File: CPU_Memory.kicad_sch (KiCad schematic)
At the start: 1 part

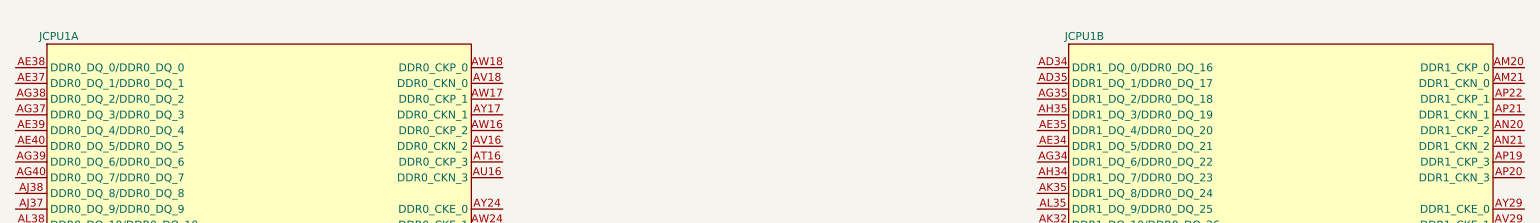
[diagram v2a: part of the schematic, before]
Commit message: Added first PCH symbol and footprint
THANKS @mothenjoyer69 so much for extracting and converting the PCH footprint from a laptop boardview ❤️
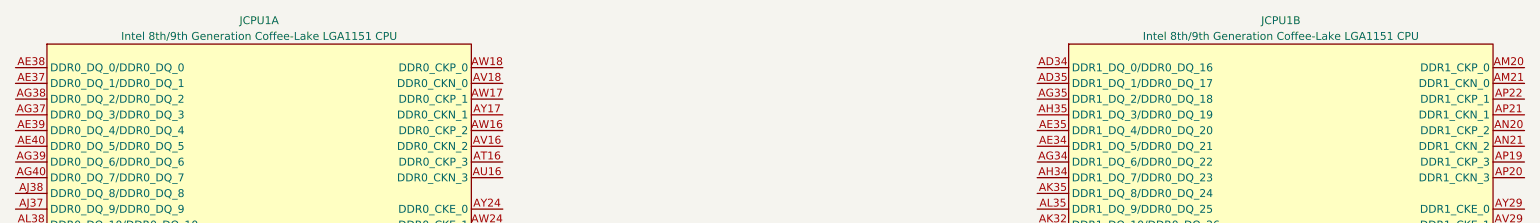
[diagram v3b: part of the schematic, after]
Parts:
- JCPU1: value ~ -> Intel 8th/9th Generation Coffee-Lake LGA1151 CPU

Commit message: Fixed some PCH pin names
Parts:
- added unit 2 of JCPU1

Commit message: Added sodimm memory slots and mostly hooked them up on the schematic
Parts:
- added JSODIMM1, JSODIMM2: DDR4-sodimm, A-my-stuff:DDR4-sodimm-std, symbol A-my-stuff:DDR4-sodimm
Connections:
- net DDR4_CH0_DQ1: now reaches JCPU1.AE37 (DDR0_DQ_1/DDR0_DQ_1)
- net DDR4_CH0_DQ1: now also JSODIMM1.7 (DQ1)
- net DDR4_CH0_DQ0: now reaches JCPU1.AE38 (DDR0_DQ_0/DDR0_DQ_0)
- net DDR4_CH0_DQ0: now also JSODIMM1.8 (DQ0)
- net DDR4_CH0_DQ4: now reaches JCPU1.AE39 (DDR0_DQ_4/DDR0_DQ_4)
- net DDR4_CH0_DQ4: now also JSODIMM1.4 (DQ4)
- net DDR4_CH0_DQ5: now reaches JCPU1.AE40 (DDR0_DQ_5/DDR0_DQ_5)
- net DDR4_CH0_DQ5: now also JSODIMM1.3 (DQ5)
- net DDR4_CH0_DQS0+: now reaches JCPU1.AF38 (DDR0_DQSP_0/DDR0_DQSP_0)
- net DDR4_CH0_DQS0+: now also JSODIMM1.13 (DQS0+)
- net DDR4_CH0_DQS0-: now reaches JCPU1.AF39 (DDR0_DQSN_0/DDR0_DQSN_0)
- net DDR4_CH0_DQS0-: now also JSODIMM1.11 (DQS0-)
- net DDR4_CH0_DQ3: now reaches JCPU1.AG37 (DDR0_DQ_3/DDR0_DQ_3)
- net DDR4_CH0_DQ3: now also JSODIMM1.21 (DQ3)
- net DDR4_CH0_DQ2: now reaches JCPU1.AG38 (DDR0_DQ_2/DDR0_DQ_2)
- net DDR4_CH0_DQ2: now also JSODIMM1.20 (DQ2)
- net DDR4_CH0_DQ6: now reaches JCPU1.AG39 (DDR0_DQ_6/DDR0_DQ_6)
- net DDR4_CH0_DQ6: now also JSODIMM1.16 (DQ6)
- net DDR4_CH0_DQ7: now reaches JCPU1.AG40 (DDR0_DQ_7/DDR0_DQ_7)
- net DDR4_CH0_DQ7: now also JSODIMM1.17 (DQ7)
- net DDR4_CH0_DQ57: now reaches JCPU1.AH1 (DDR0_DQ_57/DDR1_DQ_41)
- net DDR4_CH0_DQ57: now also JSODIMM1.236 (DQ57)
- net DDR4_CH0_DQ59: now reaches JCPU1.AH2 (DDR0_DQ_59/DDR1_DQ_43)
- net DDR4_CH0_DQ59: now also JSODIMM1.250 (DQ59)
- net DDR4_CH0_DQ62: now reaches JCPU1.AH3 (DDR0_DQ_62/DDR1_DQ_46)
- net DDR4_CH0_DQ62: now also JSODIMM1.245 (DQ62)
- net DDR4_CH0_DQ60: now reaches JCPU1.AH4 (DDR0_DQ_60/DDR1_DQ_44)
- net DDR4_CH0_DQ60: now also JSODIMM1.232 (DQ60)
- net DDR4_CH0_DQS7+: now reaches JCPU1.AJ2 (DDR0_DQSP_7/DDR1_DQSP_5)
- net DDR4_CH0_DQS7+: now also JSODIMM1.242 (DQS7+)
- net DDR4_CH0_DQS7-: now reaches JCPU1.AJ3 (DDR0_DQSN_7/DDR1_DQSN_5)
- net DDR4_CH0_DQS7-: now also JSODIMM1.240 (DQS7-)
- net DDR4_CH0_DQ9: now reaches JCPU1.AJ37 (DDR0_DQ_9/DDR0_DQ_9)
- net DDR4_CH0_DQ9: now also JSODIMM1.29 (DQ9)
- net DDR4_CH0_DQ8: now reaches JCPU1.AJ38 (DDR0_DQ_8/DDR0_DQ_8)
- net DDR4_CH0_DQ8: now also JSODIMM1.28 (DQ8)
- net DDR4_CH0_DQ13: now reaches JCPU1.AJ39 (DDR0_DQ_13/DDR0_DQ_13)
- net DDR4_CH0_DQ13: now also JSODIMM1.25 (DQ13)
- net DDR4_CH0_DQ12: now reaches JCPU1.AJ40 (DDR0_DQ_12/DDR0_DQ_12)
- net DDR4_CH0_DQ12: now also JSODIMM1.24 (DQ12)
- net DDR4_CH0_DQ63: now reaches JCPU1.AK1 (DDR0_DQ_63/DDR1_DQ_47)
- net DDR4_CH0_DQ63: now also JSODIMM1.246 (DQ63)
- net DDR4_CH0_DQ61: now reaches JCPU1.AK2 (DDR0_DQ_61/DDR1_DQ_45)
- net DDR4_CH0_DQ61: now also JSODIMM1.233 (DQ61)
- net DDR4_CH0_DQ56: now reaches JCPU1.AK3 (DDR0_DQ_56/DDR1_DQ_40)
- net DDR4_CH0_DQ56: now also JSODIMM1.237 (DQ56)
- net DDR4_CH0_DQS1+: now reaches JCPU1.AK38 (DDR0_DQSP_1/DDR0_DQSP_1)
- net DDR4_CH0_DQS1+: now also JSODIMM1.34 (DQS1+)
- net DDR4_CH0_DQS1-: now reaches JCPU1.AK39 (DDR0_DQSN_1/DDR0_DQSN_1)
- net DDR4_CH0_DQS1-: now also JSODIMM1.32 (DQS1-)
- net DDR4_CH0_DQ58: now reaches JCPU1.AK4 (DDR0_DQ_58/DDR1_DQ_42)
- net DDR4_CH0_DQ58: now also JSODIMM1.249 (DQ58)
- net DDR4_CH0_DQ11: now reaches JCPU1.AL37 (DDR0_DQ_11/DDR0_DQ_11)
- net DDR4_CH0_DQ11: now also JSODIMM1.42 (DQ11)
- net DDR4_CH0_DQ10: now reaches JCPU1.AL38 (DDR0_DQ_10/DDR0_DQ_10)
- net DDR4_CH0_DQ10: now also JSODIMM1.41 (DQ10)
- net DDR4_CH0_DQ14: now reaches JCPU1.AL39 (DDR0_DQ_14/DDR0_DQ_14)
- net DDR4_CH0_DQ14: now also JSODIMM1.38 (DQ14)
- net DDR4_CH0_DQ15: now reaches JCPU1.AL40 (DDR0_DQ_15/DDR0_DQ_15)
- net DDR4_CH0_DQ15: now also JSODIMM1.37 (DQ15)
- net DDR4_CH0_DQ55: now reaches JCPU1.AM1 (DDR0_DQ_55/DDR1_DQ_39)
- net DDR4_CH0_DQ55: now also JSODIMM1.225 (DQ55)
- net DDR4_CH0_DQ53: now reaches JCPU1.AM2 (DDR0_DQ_53/DDR1_DQ_37)
- net DDR4_CH0_DQ53: now also JSODIMM1.212 (DQ53)
- net DDR4_CH0_DQ51: now reaches JCPU1.AM3 (DDR0_DQ_51/DDR1_DQ_35)
- net DDR4_CH0_DQ51: now also JSODIMM1.229 (DQ51)
- net DDR4_CH0_DQ49: now reaches JCPU1.AM4 (DDR0_DQ_49/DDR1_DQ_33)
- net DDR4_CH0_DQ49: now also JSODIMM1.215 (DQ49)
- net DDR4_CH0_DQS6+: now reaches JCPU1.AN2 (DDR0_DQSP_6/DDR1_DQSP_4)
- net DDR4_CH0_DQS6+: now also JSODIMM1.221 (DQS6+)
- net DDR4_CH0_DQS6-: now reaches JCPU1.AN3 (DDR0_DQSN_6/DDR1_DQSN_4)
- net DDR4_CH0_DQS6-: now also JSODIMM1.219 (DQS6-)
- net DDR4_CH0_DQ21: now reaches JCPU1.AN37 (DDR0_DQ_21/DDR0_DQ_37)
- net DDR4_CH0_DQ21: now also JSODIMM1.45 (DQ21)
- net DDR4_CH0_DQ16: now reaches JCPU1.AN38 (DDR0_DQ_16/DDR0_DQ_32)
- net DDR4_CH0_DQ16: now also JSODIMM1.50 (DQ16)
- net DDR4_CH0_DQ20: now reaches JCPU1.AN39 (DDR0_DQ_20/DDR0_DQ_36)
- net DDR4_CH0_DQ20: now also JSODIMM1.46 (DQ20)
- net DDR4_CH0_DQ17: now reaches JCPU1.AN40 (DDR0_DQ_17/DDR0_DQ_33)
- net DDR4_CH0_DQ17: now also JSODIMM1.49 (DQ17)
- net DDR4_CH0_DQ54: now reaches JCPU1.AP1 (DDR0_DQ_54/DDR1_DQ_38)
- net DDR4_CH0_DQ54: now also JSODIMM1.224 (DQ54)
- net DDR4_CH0_DQ48: now reaches JCPU1.AP2 (DDR0_DQ_48/DDR1_DQ_32)
- net DDR4_CH0_DQ48: now also JSODIMM1.216 (DQ48)
- net DDR4_CH0_DQ50: now reaches JCPU1.AP3 (DDR0_DQ_50/DDR1_DQ_34)
- net DDR4_CH0_DQ50: now also JSODIMM1.228 (DQ50)
- net DDR4_CH0_DQS2+: now reaches JCPU1.AP38 (DDR0_DQSP_2/DDR0_DQSP_4)
- net DDR4_CH0_DQS2+: now also JSODIMM1.55 (DQS2+)
- net DDR4_CH0_DQS2-: now reaches JCPU1.AP39 (DDR0_DQSN_2/DDR0_DQSN_4)
- net DDR4_CH0_DQS2-: now also JSODIMM1.53 (DQS2-)
- net DDR4_CH0_DQ52: now reaches JCPU1.AP4 (DDR0_DQ_52/DDR1_DQ_36)
- net DDR4_CH0_DQ52: now also JSODIMM1.211 (DQ52)
- net DDR4_CH0_DQ19: now reaches JCPU1.AR37 (DDR0_DQ_19/DDR0_DQ_35)
- net DDR4_CH0_DQ19: now also JSODIMM1.63 (DQ19)
- net DDR4_CH0_DQ18: now reaches JCPU1.AR38 (DDR0_DQ_18/DDR0_DQ_34)
- net DDR4_CH0_DQ18: now also JSODIMM1.62 (DQ18)
- net DDR4_CH0_DQ22: now reaches JCPU1.AR39 (DDR0_DQ_22/DDR0_DQ_38)
- net DDR4_CH0_DQ22: now also JSODIMM1.58 (DQ22)
- net DDR4_CH0_DQ23: now reaches JCPU1.AR40 (DDR0_DQ_23/DDR0_DQ_39)
- net DDR4_CH0_DQ23: now also JSODIMM1.59 (DQ23)
- net DDR4_CH0_DQ42: now reaches JCPU1.AT1 (DDR0_DQ_42/DDR1_DQ_10)
- net DDR4_CH0_DQ42: now also JSODIMM1.207 (DQ42)
- net DDR4_CH0_A4: now reaches JCPU1.AT19 (DDR0_MA_4)
- net DDR4_CH0_A4: now also JSODIMM1.128 (A4)
- net DDR4_CH0_DQ43: now reaches JCPU1.AT2 (DDR0_DQ_43/DDR1_DQ_11)
- net DDR4_CH0_DQ43: now also JSODIMM1.208 (DQ43)
- net DDR4_CH0_A8: now reaches JCPU1.AT20 (DDR0_MA_8)
- net DDR4_CH0_A8: now also JSODIMM1.125 (A8)
- net DDR4_CH0_A9: now reaches JCPU1.AT22 (DDR0_MA_9)
- net DDR4_CH0_A9: now also JSODIMM1.121 (A9)
- net DDR4_CH0_Alert#: now reaches JCPU1.AT23 (DDR0_ALERT#)
- net DDR4_CH0_Alert#: now also JSODIMM1.116 (ALERT#)
- net DDR4_CH0_DQ47: now reaches JCPU1.AT3 (DDR0_DQ_47/DDR1_DQ_15)
- net DDR4_CH0_DQ47: now also JSODIMM1.204 (DQ47)
- net DDR4_CH0_ECC1: now reaches JCPU1.AT33 (DDR0_ECC_1)
- net DDR4_CH0_ECC1: now also JSODIMM1.91 (CB1)
- net DDR4_CH0_DQ30: now reaches JCPU1.AT35 (DDR0_DQ_30/DDR0_DQ_46)
- net DDR4_CH0_DQ30: now also JSODIMM1.79 (DQ30)
- net DDR4_CH0_DQ46: now reaches JCPU1.AT4 (DDR0_DQ_46/DDR1_DQ_14)
- net DDR4_CH0_DQ46: now also JSODIMM1.203 (DQ46)
- net DDR4_CH0_CS1#: now reaches JCPU1.AU11 (DDR0_CS#_1)
- net DDR4_CH0_CS1#: now also JSODIMM1.157 (CS1#)
- net DDR4_CH0_ODT1: now reaches JCPU1.AU14 (DDR0_ODT_1)
- net DDR4_CH0_ODT1: now also JSODIMM1.161 (ODT1)
- net DDR4_CH0_A2: now reaches JCPU1.AU17 (DDR0_MA_2)
- net DDR4_CH0_A2: now also JSODIMM1.132 (A2)
- net DDR4_CH0_A1: now reaches JCPU1.AU18 (DDR0_MA_1)
- net DDR4_CH0_A1: now also JSODIMM1.133 (A1)
- net DDR4_CH0_DQS5+: now reaches JCPU1.AU2 (DDR0_DQSP_5/DDR1_DQSP_1)
- net DDR4_CH0_DQS5+: now also JSODIMM1.200 (DQS5+)
- net DDR4_CH0_A5: now reaches JCPU1.AU20 (DDR0_MA_5)
- net DDR4_CH0_A5: now also JSODIMM1.126 (A5)
- net DDR4_CH0_A7: now reaches JCPU1.AU21 (DDR0_MA_7)
- net DDR4_CH0_A7: now also JSODIMM1.122 (A7)
- net DDR4_CH0_A11: now reaches JCPU1.AU22 (DDR0_MA_11)
- net DDR4_CH0_A11: now also JSODIMM1.120 (A11)
- net DDR4_CH0_ACT#: now reaches JCPU1.AU24 (DDR0_ACT#)
- net DDR4_CH0_ACT#: now also JSODIMM1.114 (ACT#)
- net DDR4_CH0_DQS5-: now reaches JCPU1.AU3 (DDR0_DQSN_5/DDR1_DQSN_1)
- net DDR4_CH0_DQS5-: now also JSODIMM1.198 (DQS5-)
- net DDR4_CH0_ECC4: now reaches JCPU1.AU31 (DDR0_ECC_4)
- net DDR4_CH0_ECC4: now also JSODIMM1.88 (CB4)
- net DDR4_CH0_DQS8-: now reaches JCPU1.AU32 (DDR0_DQSN_8/DDR0_DQSN_8)
- net DDR4_CH0_DQS8-: now also JSODIMM1.95 (DQS8-)
- net DDR4_CH0_ECC0: now reaches JCPU1.AU33 (DDR0_ECC_0)
- net DDR4_CH0_ECC0: now also JSODIMM1.92 (CB0)
- net DDR4_CH0_DQ31: now reaches JCPU1.AU35 (DDR0_DQ_31/DDR0_DQ_47)
- net DDR4_CH0_DQ31: now also JSODIMM1.80 (DQ31)
- net DDR4_CH0_DQS3-: now reaches JCPU1.AU36 (DDR0_DQSN_3/DDR0_DQSN_5)
- net DDR4_CH0_DQS3-: now also JSODIMM1.74 (DQS3-)
- net DDR4_CH0_DQ28: now reaches JCPU1.AU37 (DDR0_DQ_28/DDR0_DQ_44)
- net DDR4_CH0_DQ28: now also JSODIMM1.66 (DQ28)
- net DDR4_CH0_DQ25: now reaches JCPU1.AU38 (DDR0_DQ_25/DDR0_DQ_41)
- net DDR4_CH0_DQ25: now also JSODIMM1.71 (DQ25)
- net DDR4_CH0_DQ35: now reaches JCPU1.AU6 (DDR0_DQ_35/DDR1_DQ_3)
- net DDR4_CH0_DQ35: now also JSODIMM1.186 (DQ35)
- net DDR4_CH0_DQ36: now reaches JCPU1.AU8 (DDR0_DQ_36/DDR1_DQ_4)
- net DDR4_CH0_DQ36: now also JSODIMM1.170 (DQ36)
- net DDR4_CH0_A13: now reaches JCPU1.AV12 (DDR0_MA_13)
- net DDR4_CH0_A13: now also JSODIMM1.158 (A13)
- net DDR4_CH0_A14_WE#: now reaches JCPU1.AV14 (DDR0_MA_14)
- net DDR4_CH0_A14_WE#: now also JSODIMM1.151 (A14/WE#)
- net DDR4_CH0_BA1: now reaches JCPU1.AV15 (DDR0_BA_1)
- net DDR4_CH0_BA1: now also JSODIMM1.145 (BA1)
- net DDR4_CH0_CLK0-: now reaches JCPU1.AV18 (DDR0_CKN_0)
- net DDR4_CH0_CLK0-: now also JSODIMM1.139 (CK0-)
- net DDR4_CH0_A3: now reaches JCPU1.AV19 (DDR0_MA_3)
- net DDR4_CH0_A3: now also JSODIMM1.131 (A3)
- net DDR4_CH0_A6: now reaches JCPU1.AV20 (DDR0_MA_6)
- net DDR4_CH0_A6: now also JSODIMM1.127 (A6)
- net DDR4_CH0_A12: now reaches JCPU1.AV22 (DDR0_MA_12)
- net DDR4_CH0_A12: now also JSODIMM1.119 (A12/BC#)
- net DDR4_CH0_BG1: now reaches JCPU1.AV23 (DDR0_BG_1)
- net DDR4_CH0_BG1: now also JSODIMM1.113 (BG1)
- net DDR4_CH0_DQ44: now reaches JCPU1.AV3 (DDR0_DQ_44/DDR1_DQ_12)
- net DDR4_CH0_DQ44: now also JSODIMM1.191 (DQ44)
- net DDR4_CH0_ECC3: now reaches JCPU1.AV31 (DDR0_ECC_3)
- net DDR4_CH0_ECC3: now also JSODIMM1.105 (CB3)
- net DDR4_CH0_DQS8+: now reaches JCPU1.AV32 (DDR0_DQSP_8/DDR0_DQSP_8)
- net DDR4_CH0_DQS8+: now also JSODIMM1.97 (DQS8+)
- net DDR4_CH0_ECC5: now reaches JCPU1.AV33 (DDR0_ECC_5)
- net DDR4_CH0_ECC5: now also JSODIMM1.87 (CB5)
- net DDR4_CH0_DQ26: now reaches JCPU1.AV35 (DDR0_DQ_26/DDR0_DQ_42)
- net DDR4_CH0_DQ26: now also JSODIMM1.83 (DQ26)
- net DDR4_CH0_DQS3+: now reaches JCPU1.AV36 (DDR0_DQSP_3/DDR0_DQSP_5)
- net DDR4_CH0_DQS3+: now also JSODIMM1.76 (DQS3+)
- net DDR4_CH0_DQ29: now reaches JCPU1.AV37 (DDR0_DQ_29/DDR0_DQ_45)
- net DDR4_CH0_DQ29: now also JSODIMM1.67 (DQ29)
- net DDR4_CH0_DQ41: now reaches JCPU1.AV4 (DDR0_DQ_41/DDR1_DQ_9)
- net DDR4_CH0_DQ41: now also JSODIMM1.194 (DQ41)
- net DDR4_CH0_DQ34: now reaches JCPU1.AV6 (DDR0_DQ_34/DDR1_DQ_2)
- net DDR4_CH0_DQ34: now also JSODIMM1.187 (DQ34)
- net DDR4_CH0_DQS4+: now reaches JCPU1.AV7 (DDR0_DQSP_4/DDR1_DQSP_0)
- net DDR4_CH0_DQS4+: now also JSODIMM1.179 (DQS4+)
- net DDR4_CH0_DQ37: now reaches JCPU1.AV8 (DDR0_DQ_37/DDR1_DQ_5)
- net DDR4_CH0_DQ37: now also JSODIMM1.169 (DQ37)
- net DDR4_CH0_ODT0: now reaches JCPU1.AW11 (DDR0_ODT_0)
- net DDR4_CH0_ODT0: now also JSODIMM1.155 (ODT0)
- net DDR4_CH0_CS0#: now reaches JCPU1.AW12 (DDR0_CS#_0)
- net DDR4_CH0_CS0#: now also JSODIMM1.149 (CS0#)
- net DDR4_CH0_A16_RAS#: now reaches JCPU1.AW13 (DDR0_MA_16)
- net DDR4_CH0_A16_RAS#: now also JSODIMM1.152 (A16/RAS#)
- net DDR4_CH0_A0: now reaches JCPU1.AW15 (DDR0_MA_0)
- net DDR4_CH0_A0: now also JSODIMM1.144 (A0)
- net DDR4_CH0_CLK1+: now reaches JCPU1.AW17 (DDR0_CKP_1)
- net DDR4_CH0_CLK1+: now also JSODIMM1.138 (CK1+)
- net DDR4_CH0_CLK0+: now reaches JCPU1.AW18 (DDR0_CKP_0)
- net DDR4_CH0_CLK0+: now also JSODIMM1.137 (CK0+)
- net DDR4_CH0_BG0: now reaches JCPU1.AW23 (DDR0_BG_0)
- net DDR4_CH0_BG0: now also JSODIMM1.115 (BG0)
- net DDR4_CH0_CKE1: now reaches JCPU1.AW24 (DDR0_CKE_1)
- net DDR4_CH0_CKE1: now also JSODIMM1.110 (CKE1)
- net DDR4_CH0_ECC6: now reaches JCPU1.AW31 (DDR0_ECC_6)
- net DDR4_CH0_ECC6: now also JSODIMM1.100 (CB6)
- net DDR4_CH0_ECC2: now reaches JCPU1.AW33 (DDR0_ECC_2)
- net DDR4_CH0_ECC2: now also JSODIMM1.101 (CB2)
- net DDR4_CH0_DQ27: now reaches JCPU1.AW35 (DDR0_DQ_27/DDR0_DQ_43)
- net DDR4_CH0_DQ27: now also JSODIMM1.84 (DQ27)
- net DDR4_CH0_DQ24: now reaches JCPU1.AW37 (DDR0_DQ_24/DDR0_DQ_40)
- net DDR4_CH0_DQ24: now also JSODIMM1.70 (DQ24)
- net DDR4_CH0_DQ45: now reaches JCPU1.AW4 (DDR0_DQ_45/DDR1_DQ_13)
- net DDR4_CH0_DQ45: now also JSODIMM1.190 (DQ45)
- net DDR4_CH0_DQ38: now reaches JCPU1.AW6 (DDR0_DQ_38/DDR1_DQ_6)
- net DDR4_CH0_DQ38: now also JSODIMM1.183 (DQ38)
- net DDR4_CH0_DQS4-: now reaches JCPU1.AW7 (DDR0_DQSN_4/DDR1_DQSN_0)
- net DDR4_CH0_DQS4-: now also JSODIMM1.177 (DQS4-)
- net DDR4_CH0_DQ33: now reaches JCPU1.AW8 (DDR0_DQ_33/DDR1_DQ_1)
- net DDR4_CH0_DQ33: now also JSODIMM1.173 (DQ33)
- net DDR4_CH0_A15_CAS#: now reaches JCPU1.AY11 (DDR0_MA_15)
- net DDR4_CH0_A15_CAS#: now also JSODIMM1.156 (A15/CAS#)
- net DDR4_CH0_BA0: now reaches JCPU1.AY13 (DDR0_BA_0)
- net DDR4_CH0_BA0: now also JSODIMM1.150 (BA0)
- net DDR4_CH0_A10: now reaches JCPU1.AY14 (DDR0_MA_10)
- net DDR4_CH0_A10: now also JSODIMM1.146 (A10/AP)
- net DDR4_CH0_Parity: now reaches JCPU1.AY15 (DDR0_PAR)
- net DDR4_CH0_Parity: now also JSODIMM1.143 (PARITY)
- net DDR4_CH0_CLK1-: now reaches JCPU1.AY17 (DDR0_CKN_1)
- net DDR4_CH0_CLK1-: now also JSODIMM1.140 (CK1-)
- net DDR4_CH0_CKE0: now reaches JCPU1.AY24 (DDR0_CKE_0)
- net DDR4_CH0_CKE0: now also JSODIMM1.109 (CKE0)
- net DDR4_CH0_ECC7: now reaches JCPU1.AY31 (DDR0_ECC_7)
- net DDR4_CH0_ECC7: now also JSODIMM1.104 (CB7)
- net DDR4_CH0_DQ40: now reaches JCPU1.AY4 (DDR0_DQ_40/DDR1_DQ_8)
- net DDR4_CH0_DQ40: now also JSODIMM1.195 (DQ40)
- net DDR4_CH0_DQ39: now reaches JCPU1.AY6 (DDR0_DQ_39/DDR1_DQ_7)
- net DDR4_CH0_DQ39: now also JSODIMM1.182 (DQ39)
- net DDR4_CH0_DQ32: now reaches JCPU1.AY8 (DDR0_DQ_32/DDR1_DQ_0)
- net DDR4_CH0_DQ32: now also JSODIMM1.174 (DQ32)
- net DDR4_CH1_DQ0: now reaches JCPU1.AD34 (DDR1_DQ_0/DDR0_DQ_16)
- net DDR4_CH1_DQ0: now also JSODIMM2.8 (DQ0)
- net DDR4_CH1_DQ1: now reaches JCPU1.AD35 (DDR1_DQ_1/DDR0_DQ_17)
- net DDR4_CH1_DQ1: now also JSODIMM2.7 (DQ1)
- net DDR4_CH1_DQ5: now reaches JCPU1.AE34 (DDR1_DQ_5/DDR0_DQ_21)
- net DDR4_CH1_DQ5: now also JSODIMM2.3 (DQ5)
- net DDR4_CH1_DQ4: now reaches JCPU1.AE35 (DDR1_DQ_4/DDR0_DQ_20)
- net DDR4_CH1_DQ4: now also JSODIMM2.4 (DQ4)
- net DDR4_CH1_DQ58: now reaches JCPU1.AE6 (DDR1_DQ_58/DDR1_DQ_58)
- net DDR4_CH1_DQ58: now also JSODIMM2.249 (DQ58)
- net DDR4_CH1_DQ62: now reaches JCPU1.AE7 (DDR1_DQ_62/DDR1_DQ_62)
- net DDR4_CH1_DQ62: now also JSODIMM2.245 (DQ62)
- net DDR4_CH1_DQS0-: now reaches JCPU1.AF34 (DDR1_DQSN_0/DDR0_DQSN_2)
- net DDR4_CH1_DQS0-: now also JSODIMM2.11 (DQS0-)
- net DDR4_CH1_DQS0+: now reaches JCPU1.AF35 (DDR1_DQSP_0/DDR0_DQSP_2)
- net DDR4_CH1_DQS0+: now also JSODIMM2.13 (DQS0+)
- net DDR4_CH1_DQ63: now reaches JCPU1.AF6 (DDR1_DQ_63/DDR1_DQ_63)
- net DDR4_CH1_DQ63: now also JSODIMM2.246 (DQ63)
- net DDR4_CH1_DQ59: now reaches JCPU1.AF7 (DDR1_DQ_59/DDR1_DQ_59)
- net DDR4_CH1_DQ59: now also JSODIMM2.250 (DQ59)
- net DDR4_CH1_DQ6: now reaches JCPU1.AG34 (DDR1_DQ_6/DDR0_DQ_22)
- net DDR4_CH1_DQ6: now also JSODIMM2.16 (DQ6)
- net DDR4_CH1_DQ2: now reaches JCPU1.AG35 (DDR1_DQ_2/DDR0_DQ_18)
- net DDR4_CH1_DQ2: now also JSODIMM2.20 (DQ2)
- net DDR4_CH1_DQS7-: now reaches JCPU1.AG6 (DDR1_DQSN_7/DDR1_DQSN_7)
- net DDR4_CH1_DQS7-: now also JSODIMM2.240 (DQS7-)
- net DDR4_CH1_DQS7+: now reaches JCPU1.AG7 (DDR1_DQSP_7/DDR1_DQSP_7)
- net DDR4_CH1_DQS7+: now also JSODIMM2.242 (DQS7+)
- net DDR4_CH1_DQ7: now reaches JCPU1.AH34 (DDR1_DQ_7/DDR0_DQ_23)
- net DDR4_CH1_DQ7: now also JSODIMM2.17 (DQ7)
- net DDR4_CH1_DQ3: now reaches JCPU1.AH35 (DDR1_DQ_3/DDR0_DQ_19)
- net DDR4_CH1_DQ3: now also JSODIMM2.21 (DQ3)
- net DDR4_CH1_DQ61: now reaches JCPU1.AH6 (DDR1_DQ_61/DDR1_DQ_61)
- net DDR4_CH1_DQ61: now also JSODIMM2.233 (DQ61)
- net DDR4_CH1_DQ60: now reaches JCPU1.AH7 (DDR1_DQ_60/DDR1_DQ_60)
- net DDR4_CH1_DQ60: now also JSODIMM2.232 (DQ60)
- net DDR4_CH1_DQ56: now reaches JCPU1.AJ6 (DDR1_DQ_56/DDR1_DQ_56)
- net DDR4_CH1_DQ56: now also JSODIMM2.237 (DQ56)
- net DDR4_CH1_DQ57: now reaches JCPU1.AJ7 (DDR1_DQ_57/DDR1_DQ_57)
- net DDR4_CH1_DQ57: now also JSODIMM2.236 (DQ57)
- net DDR4_CH1_DQ14: now reaches JCPU1.AK31 (DDR1_DQ_14/DDR0_DQ_30)
- net DDR4_CH1_DQ14: now also JSODIMM2.38 (DQ14)
- net DDR4_CH1_DQ10: now reaches JCPU1.AK32 (DDR1_DQ_10/DDR0_DQ_26)
- net DDR4_CH1_DQ10: now also JSODIMM2.41 (DQ10)
- net DDR4_CH1_DQS1-: now reaches JCPU1.AK33 (DDR1_DQSN_1/DDR0_DQSN_3)
- net DDR4_CH1_DQS1-: now also JSODIMM2.32 (DQS1-)
- net DDR4_CH1_DQ12: now reaches JCPU1.AK34 (DDR1_DQ_12/DDR0_DQ_28)
- net DDR4_CH1_DQ12: now also JSODIMM2.24 (DQ12)
- net DDR4_CH1_DQ8: now reaches JCPU1.AK35 (DDR1_DQ_8/DDR0_DQ_24)
- net DDR4_CH1_DQ8: now also JSODIMM2.28 (DQ8)
- net DDR4_CH1_DQ49: now reaches JCPU1.AL10 (DDR1_DQ_49/DDR1_DQ_49)
- net DDR4_CH1_DQ49: now also JSODIMM2.215 (DQ49)
- net DDR4_CH1_DQ39: now reaches JCPU1.AL12 (DDR1_DQ_39/DDR1_DQ_23)
- net DDR4_CH1_DQ39: now also JSODIMM2.182 (DQ39)
- net DDR4_CH1_DQ35: now reaches JCPU1.AL13 (DDR1_DQ_35/DDR1_DQ_19)
- net DDR4_CH1_DQ35: now also JSODIMM2.186 (DQ35)
- net DDR4_CH1_ODT1: now reaches JCPU1.AL16 (DDR1_ODT_1)
- net DDR4_CH1_ODT1: now also JSODIMM2.161 (ODT1)
- net DDR4_CH1_A14_WE#: now reaches JCPU1.AL17 (DDR1_MA_14)
- net DDR4_CH1_A14_WE#: now also JSODIMM2.151 (A14/WE#)
- net DDR4_CH1_BA0: now reaches JCPU1.AL18 (DDR1_BA_0)
- net DDR4_CH1_BA0: now also JSODIMM2.150 (BA0)
- net DDR4_CH1_A0: now reaches JCPU1.AL19 (DDR1_MA_0)
- net DDR4_CH1_A0: now also JSODIMM2.144 (A0)
- net DDR4_CH1_Parity: now reaches JCPU1.AL20 (DDR1_PAR)
- net DDR4_CH1_Parity: now also JSODIMM2.143 (PARITY)
- net DDR4_CH1_A1: now reaches JCPU1.AL22 (DDR1_MA_1)
- net DDR4_CH1_A1: now also JSODIMM2.133 (A1)
- net DDR4_CH1_A5: now reaches JCPU1.AL23 (DDR1_MA_5)
- net DDR4_CH1_A5: now also JSODIMM2.126 (A5)
- net DDR4_CH1_ECC6: now reaches JCPU1.AL25 (DDR1_ECC_6)
- net DDR4_CH1_ECC6: now also JSODIMM2.100 (CB6)
- net DDR4_CH1_ECC7: now reaches JCPU1.AL26 (DDR1_ECC_7)
- net DDR4_CH1_ECC7: now also JSODIMM2.104 (CB7)
- net DDR4_CH1_DQ29: now reaches JCPU1.AL28 (DDR1_DQ_29/DDR0_DQ_61)
- net DDR4_CH1_DQ29: now also JSODIMM2.67 (DQ29)
- net DDR4_CH1_DQ24: now reaches JCPU1.AL29 (DDR1_DQ_24/DDR0_DQ_56)
- net DDR4_CH1_DQ24: now also JSODIMM2.70 (DQ24)
- net DDR4_CH1_DQ15: now reaches JCPU1.AL31 (DDR1_DQ_15/DDR0_DQ_31)
- net DDR4_CH1_DQ15: now also JSODIMM2.37 (DQ15)
- net DDR4_CH1_DQ11: now reaches JCPU1.AL32 (DDR1_DQ_11/DDR0_DQ_27)
- net DDR4_CH1_DQ11: now also JSODIMM2.42 (DQ11)
- net DDR4_CH1_DQS1+: now reaches JCPU1.AL33 (DDR1_DQSP_1/DDR0_DQSP_3)
- net DDR4_CH1_DQS1+: now also JSODIMM2.34 (DQS1+)
- net DDR4_CH1_DQ13: now reaches JCPU1.AL34 (DDR1_DQ_13/DDR0_DQ_29)
- net DDR4_CH1_DQ13: now also JSODIMM2.25 (DQ13)
- net DDR4_CH1_DQ9: now reaches JCPU1.AL35 (DDR1_DQ_9/DDR0_DQ_25)
- net DDR4_CH1_DQ9: now also JSODIMM2.29 (DQ9)
- net DDR4_CH1_DQ55: now reaches JCPU1.AL6 (DDR1_DQ_55/DDR1_DQ_55)
- net DDR4_CH1_DQ55: now also JSODIMM2.225 (DQ55)
- net DDR4_CH1_DQ51: now reaches JCPU1.AL7 (DDR1_DQ_51/DDR1_DQ_51)
- net DDR4_CH1_DQ51: now also JSODIMM2.229 (DQ51)
- net DDR4_CH1_DQS6+: now reaches JCPU1.AL8 (DDR1_DQSP_6/DDR1_DQSP_6)
- net DDR4_CH1_DQS6+: now also JSODIMM2.221 (DQS6+)
- net DDR4_CH1_DQ53: now reaches JCPU1.AL9 (DDR1_DQ_53/DDR1_DQ_53)
- net DDR4_CH1_DQ53: now also JSODIMM2.212 (DQ53)
- net DDR4_CH1_DQ48: now reaches JCPU1.AM10 (DDR1_DQ_48/DDR1_DQ_48)
- net DDR4_CH1_DQ48: now also JSODIMM2.216 (DQ48)
- net DDR4_CH1_DQ38: now reaches JCPU1.AM12 (DDR1_DQ_38/DDR1_DQ_22)
- net DDR4_CH1_DQ38: now also JSODIMM2.183 (DQ38)
- net DDR4_CH1_DQ34: now reaches JCPU1.AM13 (DDR1_DQ_34/DDR1_DQ_18)
- net DDR4_CH1_DQ34: now also JSODIMM2.187 (DQ34)
- net DDR4_CH1_ODT0: now reaches JCPU1.AM16 (DDR1_ODT_0)
- net DDR4_CH1_ODT0: now also JSODIMM2.155 (ODT0)
- net DDR4_CH1_BA1: now reaches JCPU1.AM18 (DDR1_BA_1)
- net DDR4_CH1_BA1: now also JSODIMM2.145 (BA1)
- net DDR4_CH1_CLK0+: now reaches JCPU1.AM20 (DDR1_CKP_0)
- net DDR4_CH1_CLK0+: now also JSODIMM2.137 (CK0+)
- net DDR4_CH1_CLK0-: now reaches JCPU1.AM21 (DDR1_CKN_0)
- net DDR4_CH1_CLK0-: now also JSODIMM2.139 (CK0-)
- net DDR4_CH1_A2: now reaches JCPU1.AM22 (DDR1_MA_2)
- net DDR4_CH1_A2: now also JSODIMM2.132 (A2)
- net DDR4_CH1_A3: now reaches JCPU1.AM23 (DDR1_MA_3)
- net DDR4_CH1_A3: now also JSODIMM2.131 (A3)
- net DDR4_CH1_ECC3: now reaches JCPU1.AM25 (DDR1_ECC_3)
- net DDR4_CH1_ECC3: now also JSODIMM2.105 (CB3)
- net DDR4_CH1_ECC2: now reaches JCPU1.AM26 (DDR1_ECC_2)
- net DDR4_CH1_ECC2: now also JSODIMM2.101 (CB2)
- net DDR4_CH1_DQ28: now reaches JCPU1.AM28 (DDR1_DQ_28/DDR0_DQ_60)
- net DDR4_CH1_DQ28: now also JSODIMM2.66 (DQ28)
- net DDR4_CH1_DQ25: now reaches JCPU1.AM29 (DDR1_DQ_25/DDR0_DQ_57)
- net DDR4_CH1_DQ25: now also JSODIMM2.71 (DQ25)
- net DDR4_CH1_DQ54: now reaches JCPU1.AM6 (DDR1_DQ_54/DDR1_DQ_54)
- net DDR4_CH1_DQ54: now also JSODIMM2.224 (DQ54)
- net DDR4_CH1_DQ50: now reaches JCPU1.AM7 (DDR1_DQ_50/DDR1_DQ_50)
- net DDR4_CH1_DQ50: now also JSODIMM2.228 (DQ50)
- net DDR4_CH1_DQS6-: now reaches JCPU1.AM8 (DDR1_DQSN_6/DDR1_DQSN_6)
- net DDR4_CH1_DQS6-: now also JSODIMM2.219 (DQS6-)
- net DDR4_CH1_DQ52: now reaches JCPU1.AM9 (DDR1_DQ_52/DDR1_DQ_52)
- net DDR4_CH1_DQ52: now also JSODIMM2.211 (DQ52)
- net DDR4_CH1_DQS4+: now reaches JCPU1.AN12 (DDR1_DQSP_4/DDR1_DQSP_2)
- net DDR4_CH1_DQS4+: now also JSODIMM2.179 (DQS4+)
- net DDR4_CH1_DQS4-: now reaches JCPU1.AN13 (DDR1_DQSN_4/DDR1_DQSN_2)
- net DDR4_CH1_DQS4-: now also JSODIMM2.177 (DQS4-)
- net DDR4_CH1_CS1#: now reaches JCPU1.AN15 (DDR1_CS#_1)
- net DDR4_CH1_CS1#: now also JSODIMM2.157 (CS1#)
- net DDR4_CH1_A16_RAS#: now reaches JCPU1.AN18 (DDR1_MA_16)
- net DDR4_CH1_A16_RAS#: now also JSODIMM2.152 (A16/RAS#)
- net DDR4_CH1_DQS8+: now reaches JCPU1.AN25 (DDR1_DQSP_8/DDR1_DQSP_8)
- net DDR4_CH1_DQS8+: now also JSODIMM2.97 (DQS8+)
- net DDR4_CH1_DQS8-: now reaches JCPU1.AN26 (DDR1_DQSN_8/DDR1_DQSN_8)
- net DDR4_CH1_DQS8-: now also JSODIMM2.95 (DQS8-)
- net DDR4_CH1_DQS3+: now reaches JCPU1.AN28 (DDR1_DQSP_3/DDR0_DQSP_7)
- net DDR4_CH1_DQS3+: now also JSODIMM2.76 (DQS3+)
- net DDR4_CH1_DQS3-: now reaches JCPU1.AN29 (DDR1_DQSN_3/DDR0_DQSN_7)
- net DDR4_CH1_DQS3-: now also JSODIMM2.74 (DQS3-)
- net DDR4_CH1_DQ22: now reaches JCPU1.AN31 (DDR1_DQ_22/DDR0_DQ_54)
- net DDR4_CH1_DQ22: now also JSODIMM2.58 (DQ22)
- net DDR4_CH1_DQ18: now reaches JCPU1.AN32 (DDR1_DQ_18/DDR0_DQ_50)
- net DDR4_CH1_DQ18: now also JSODIMM2.62 (DQ18)
- net DDR4_CH1_DQS2-: now reaches JCPU1.AN33 (DDR1_DQSN_2/DDR0_DQSN_6)
- net DDR4_CH1_DQS2-: now also JSODIMM2.53 (DQS2-)
- net DDR4_CH1_DQ20: now reaches JCPU1.AN34 (DDR1_DQ_20/DDR0_DQ_52)
- net DDR4_CH1_DQ20: now also JSODIMM2.46 (DQ20)
- net DDR4_CH1_DQ17: now reaches JCPU1.AN35 (DDR1_DQ_17/DDR0_DQ_49)
- net DDR4_CH1_DQ17: now also JSODIMM2.49 (DQ17)
- net DDR4_CH1_DQ40: now reaches JCPU1.AP10 (DDR1_DQ_40/DDR1_DQ_24)
- net DDR4_CH1_DQ40: now also JSODIMM2.195 (DQ40)
- net DDR4_CH1_DQ33: now reaches JCPU1.AP12 (DDR1_DQ_33/DDR1_DQ_17)
- net DDR4_CH1_DQ33: now also JSODIMM2.173 (DQ33)
- net DDR4_CH1_DQ37: now reaches JCPU1.AP13 (DDR1_DQ_37/DDR1_DQ_21)
- net DDR4_CH1_DQ37: now also JSODIMM2.169 (DQ37)
- net DDR4_CH1_A15_CAS#: now reaches JCPU1.AP16 (DDR1_MA_15)
- net DDR4_CH1_A15_CAS#: now also JSODIMM2.156 (A15/CAS#)
- net DDR4_CH1_CS0#: now reaches JCPU1.AP17 (DDR1_CS#_0)
- net DDR4_CH1_CS0#: now also JSODIMM2.149 (CS0#)
- net DDR4_CH1_A10: now reaches JCPU1.AP18 (DDR1_MA_10)
- net DDR4_CH1_A10: now also JSODIMM2.146 (A10/AP)
- net DDR4_CH1_CLK1-: now reaches JCPU1.AP21 (DDR1_CKN_1)
- net DDR4_CH1_CLK1-: now also JSODIMM2.140 (CK1-)
- net DDR4_CH1_CLK1+: now reaches JCPU1.AP22 (DDR1_CKP_1)
- net DDR4_CH1_CLK1+: now also JSODIMM2.138 (CK1+)
- net DDR4_CH1_A4: now reaches JCPU1.AP23 (DDR1_MA_4)
- net DDR4_CH1_A4: now also JSODIMM2.128 (A4)
- net DDR4_CH1_ECC5: now reaches JCPU1.AP25 (DDR1_ECC_5)
- net DDR4_CH1_ECC5: now also JSODIMM2.87 (CB5)
- net DDR4_CH1_ECC4: now reaches JCPU1.AP26 (DDR1_ECC_4)
- net DDR4_CH1_ECC4: now also JSODIMM2.88 (CB4)
- net DDR4_CH1_DQ31: now reaches JCPU1.AP28 (DDR1_DQ_31/DDR0_DQ_63)
- net DDR4_CH1_DQ31: now also JSODIMM2.80 (DQ31)
- net DDR4_CH1_DQ26: now reaches JCPU1.AP29 (DDR1_DQ_26/DDR0_DQ_58)
- net DDR4_CH1_DQ26: now also JSODIMM2.83 (DQ26)
- net DDR4_CH1_DQ23: now reaches JCPU1.AP31 (DDR1_DQ_23/DDR0_DQ_55)
- net DDR4_CH1_DQ23: now also JSODIMM2.59 (DQ23)
- net DDR4_CH1_DQ19: now reaches JCPU1.AP32 (DDR1_DQ_19/DDR0_DQ_51)
- net DDR4_CH1_DQ19: now also JSODIMM2.63 (DQ19)
- net DDR4_CH1_DQS2+: now reaches JCPU1.AP33 (DDR1_DQSP_2/DDR0_DQSP_6)
- net DDR4_CH1_DQS2+: now also JSODIMM2.55 (DQS2+)
- net DDR4_CH1_DQ21: now reaches JCPU1.AP34 (DDR1_DQ_21/DDR0_DQ_53)
- net DDR4_CH1_DQ21: now also JSODIMM2.45 (DQ21)
- net DDR4_CH1_DQ16: now reaches JCPU1.AP35 (DDR1_DQ_16/DDR0_DQ_48)
- net DDR4_CH1_DQ16: now also JSODIMM2.50 (DQ16)
- net DDR4_CH1_DQ47: now reaches JCPU1.AP6 (DDR1_DQ_47/DDR1_DQ_31)
- net DDR4_CH1_DQ47: now also JSODIMM2.204 (DQ47)
- net DDR4_CH1_DQ43: now reaches JCPU1.AP7 (DDR1_DQ_43/DDR1_DQ_27)
- net DDR4_CH1_DQ43: now also JSODIMM2.208 (DQ43)
- net DDR4_CH1_DQS5+: now reaches JCPU1.AP8 (DDR1_DQSP_5/DDR1_DQSP_3)
- net DDR4_CH1_DQS5+: now also JSODIMM2.200 (DQS5+)
- net DDR4_CH1_DQ45: now reaches JCPU1.AP9 (DDR1_DQ_45/DDR1_DQ_29)
- net DDR4_CH1_DQ45: now also JSODIMM2.190 (DQ45)
- net DDR4_CH1_DQ41: now reaches JCPU1.AR10 (DDR1_DQ_41/DDR1_DQ_25)
- net DDR4_CH1_DQ41: now also JSODIMM2.194 (DQ41)
- net DDR4_CH1_DQ32: now reaches JCPU1.AR12 (DDR1_DQ_32/DDR1_DQ_16)
- net DDR4_CH1_DQ32: now also JSODIMM2.174 (DQ32)
- net DDR4_CH1_DQ36: now reaches JCPU1.AR13 (DDR1_DQ_36/DDR1_DQ_20)
- net DDR4_CH1_DQ36: now also JSODIMM2.170 (DQ36)
- net DDR4_CH1_A13: now reaches JCPU1.AR15 (DDR1_MA_13)
- net DDR4_CH1_A13: now also JSODIMM2.158 (A13)
- net DDR4_CH1_ECC0: now reaches JCPU1.AR25 (DDR1_ECC_0)
- net DDR4_CH1_ECC0: now also JSODIMM2.92 (CB0)
- net DDR4_CH1_ECC1: now reaches JCPU1.AR26 (DDR1_ECC_1)
- net DDR4_CH1_ECC1: now also JSODIMM2.91 (CB1)
- net DDR4_CH1_DQ30: now reaches JCPU1.AR28 (DDR1_DQ_30/DDR0_DQ_62)
- net DDR4_CH1_DQ30: now also JSODIMM2.79 (DQ30)
- net DDR4_CH1_DQ27: now reaches JCPU1.AR29 (DDR1_DQ_27/DDR0_DQ_59)
- net DDR4_CH1_DQ27: now also JSODIMM2.84 (DQ27)
- net DDR4_CH1_DQ46: now reaches JCPU1.AR6 (DDR1_DQ_46/DDR1_DQ_30)
- net DDR4_CH1_DQ46: now also JSODIMM2.203 (DQ46)
- net DDR4_CH1_DQ42: now reaches JCPU1.AR7 (DDR1_DQ_42/DDR1_DQ_26)
- net DDR4_CH1_DQ42: now also JSODIMM2.207 (DQ42)
- net DDR4_CH1_DQS5-: now reaches JCPU1.AR8 (DDR1_DQSN_5/DDR1_DQSN_3)
- net DDR4_CH1_DQS5-: now also JSODIMM2.198 (DQS5-)
- net DDR4_CH1_DQ44: now reaches JCPU1.AR9 (DDR1_DQ_44/DDR1_DQ_28)
- net DDR4_CH1_DQ44: now also JSODIMM2.191 (DQ44)
- net DDR4_CH1_A8: now reaches JCPU1.AU26 (DDR1_MA_8)
- net DDR4_CH1_A8: now also JSODIMM2.125 (A8)
- net DDR4_CH1_A11: now reaches JCPU1.AU27 (DDR1_MA_11)
- net DDR4_CH1_A11: now also JSODIMM2.120 (A11)
- net DDR4_CH1_ACT#: now reaches JCPU1.AU28 (DDR1_ACT#)
- net DDR4_CH1_ACT#: now also JSODIMM2.114 (ACT#)
- net DDR4_CH1_A12: now reaches JCPU1.AV27 (DDR1_MA_12)
- net DDR4_CH1_A12: now also JSODIMM2.119 (A12/BC#)
- net DDR4_CH1_CKE1: now reaches JCPU1.AV29 (DDR1_CKE_1)
- net DDR4_CH1_CKE1: now also JSODIMM2.110 (CKE1)
- net DDR4_CH1_A6: now reaches JCPU1.AW26 (DDR1_MA_6)
- net DDR4_CH1_A6: now also JSODIMM2.127 (A6)
- net DDR4_CH1_A9: now reaches JCPU1.AW27 (DDR1_MA_9)
- net DDR4_CH1_A9: now also JSODIMM2.121 (A9)
- net DDR4_CH1_BG0: now reaches JCPU1.AW28 (DDR1_BG_0)
- net DDR4_CH1_BG0: now also JSODIMM2.115 (BG0)
- net DDR4_CH1_Alert#: now reaches JCPU1.AY25 (DDR1_ALERT#)
- net DDR4_CH1_Alert#: now also JSODIMM2.116 (ALERT#)
- net DDR4_CH1_A7: now reaches JCPU1.AY26 (DDR1_MA_7)
- net DDR4_CH1_A7: now also JSODIMM2.122 (A7)
- net DDR4_CH1_BG1: now reaches JCPU1.AY28 (DDR1_BG_1)
- net DDR4_CH1_BG1: now also JSODIMM2.113 (BG1)
- net DDR4_CH1_CKE0: now reaches JCPU1.AY29 (DDR1_CKE_0)
- net DDR4_CH1_CKE0: now also JSODIMM2.109 (CKE0)

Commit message: Added pretty colors
pretty fun to do
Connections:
- net GND: now reaches JSODIMM2.1 (VSS)
- net GND: now also JSODIMM1.1 (VSS), JSODIMM1.10 (VSS), JSODIMM1.102 (VSS), JSODIMM1.103 (VSS), JSODIMM1.106 (VSS), JSODIMM1.107 (VSS), JSODIMM1.14 (VSS), JSODIMM1.15 (VSS), JSODIMM1.167 (VSS), JSODIMM1.168 (VSS), JSODIMM1.171 (VSS), JSODIMM1.172 (VSS), JSODIMM1.175 (VSS), JSODIMM1.176 (VSS), JSODIMM1.18 (VSS), JSODIMM1.180 (VSS), JSODIMM1.181 (VSS), JSODIMM1.184 (VSS), JSODIMM1.185 (VSS), JSODIMM1.188 (VSS), JSODIMM1.189 (VSS), JSODIMM1.19 (VSS), JSODIMM1.192 (VSS), JSODIMM1.193 (VSS), JSODIMM1.196 (VSS), JSODIMM1.197 (VSS), JSODIMM1.2 (VSS), JSODIMM1.201 (VSS), JSODIMM1.202 (VSS), JSODIMM1.205 (VSS), JSODIMM1.206 (VSS), JSODIMM1.209 (VSS), JSODIMM1.210 (VSS), JSODIMM1.213 (VSS), JSODIMM1.214 (VSS), JSODIMM1.217 (VSS), JSODIMM1.218 (VSS), JSODIMM1.22 (VSS), JSODIMM1.222 (VSS), JSODIMM1.223 (VSS), JSODIMM1.226 (VSS), JSODIMM1.227 (VSS), JSODIMM1.23 (VSS), JSODIMM1.230 (VSS), JSODIMM1.231 (VSS), JSODIMM1.234 (VSS), JSODIMM1.235 (VSS), JSODIMM1.238 (VSS), JSODIMM1.239 (VSS), JSODIMM1.243 (VSS), JSODIMM1.244 (VSS), JSODIMM1.247 (VSS), JSODIMM1.248 (VSS), JSODIMM1.251 (VSS), JSODIMM1.252 (VSS), JSODIMM1.26 (VSS), JSODIMM1.27 (VSS), JSODIMM1.30 (VSS), JSODIMM1.31 (VSS), JSODIMM1.35 (VSS), JSODIMM1.36 (VSS), JSODIMM1.39 (VSS), JSODIMM1.40 (VSS), JSODIMM1.43 (VSS), JSODIMM1.44 (VSS), JSODIMM1.47 (VSS), JSODIMM1.48 (VSS), JSODIMM1.5 (VSS), JSODIMM1.51 (VSS), JSODIMM1.52 (VSS), JSODIMM1.56 (VSS), JSODIMM1.57 (VSS), JSODIMM1.6 (VSS), JSODIMM1.60 (VSS), JSODIMM1.61 (VSS), JSODIMM1.64 (VSS), JSODIMM1.65 (VSS), JSODIMM1.68 (VSS), JSODIMM1.69 (VSS), JSODIMM1.72 (VSS), JSODIMM1.73 (VSS), JSODIMM1.77 (VSS), JSODIMM1.78 (VSS), JSODIMM1.81 (VSS), JSODIMM1.82 (VSS), JSODIMM1.85 (VSS), JSODIMM1.86 (VSS), JSODIMM1.89 (VSS), JSODIMM1.9 (VSS), JSODIMM1.90 (VSS), JSODIMM1.93 (VSS), JSODIMM1.94 (VSS), JSODIMM1.98 (VSS), JSODIMM1.99 (VSS), JSODIMM1.MP1, JSODIMM1.MP2, JSODIMM2.10 (VSS), JSODIMM2.102 (VSS), JSODIMM2.103 (VSS), JSODIMM2.106 (VSS), JSODIMM2.107 (VSS), JSODIMM2.14 (VSS), JSODIMM2.15 (VSS), JSODIMM2.167 (VSS), JSODIMM2.168 (VSS), JSODIMM2.171 (VSS), JSODIMM2.172 (VSS), JSODIMM2.175 (VSS), JSODIMM2.176 (VSS), JSODIMM2.18 (VSS), JSODIMM2.180 (VSS), JSODIMM2.181 (VSS), JSODIMM2.184 (VSS), JSODIMM2.185 (VSS), JSODIMM2.188 (VSS), JSODIMM2.189 (VSS), JSODIMM2.19 (VSS), JSODIMM2.192 (VSS), JSODIMM2.193 (VSS), JSODIMM2.196 (VSS), JSODIMM2.197 (VSS), JSODIMM2.2 (VSS), JSODIMM2.201 (VSS), JSODIMM2.202 (VSS), JSODIMM2.205 (VSS), JSODIMM2.206 (VSS), JSODIMM2.209 (VSS), JSODIMM2.210 (VSS), JSODIMM2.213 (VSS), JSODIMM2.214 (VSS), JSODIMM2.217 (VSS), JSODIMM2.218 (VSS), JSODIMM2.22 (VSS), JSODIMM2.222 (VSS), JSODIMM2.223 (VSS), JSODIMM2.226 (VSS), JSODIMM2.227 (VSS), JSODIMM2.23 (VSS), JSODIMM2.230 (VSS), JSODIMM2.231 (VSS), JSODIMM2.234 (VSS), JSODIMM2.235 (VSS), JSODIMM2.238 (VSS), JSODIMM2.239 (VSS), JSODIMM2.243 (VSS), JSODIMM2.244 (VSS), JSODIMM2.247 (VSS), JSODIMM2.248 (VSS), JSODIMM2.251 (VSS), JSODIMM2.252 (VSS), JSODIMM2.26 (VSS), JSODIMM2.27 (VSS), JSODIMM2.30 (VSS), JSODIMM2.31 (VSS), JSODIMM2.35 (VSS), JSODIMM2.36 (VSS), JSODIMM2.39 (VSS), JSODIMM2.40 (VSS), JSODIMM2.43 (VSS), JSODIMM2.44 (VSS), JSODIMM2.47 (VSS), JSODIMM2.48 (VSS), JSODIMM2.5 (VSS), JSODIMM2.51 (VSS), JSODIMM2.52 (VSS), JSODIMM2.56 (VSS), JSODIMM2.57 (VSS), JSODIMM2.6 (VSS), JSODIMM2.60 (VSS), JSODIMM2.61 (VSS), JSODIMM2.64 (VSS), JSODIMM2.65 (VSS), JSODIMM2.68 (VSS), JSODIMM2.69 (VSS), JSODIMM2.72 (VSS), JSODIMM2.73 (VSS), JSODIMM2.77 (VSS), JSODIMM2.78 (VSS), JSODIMM2.81 (VSS), JSODIMM2.82 (VSS), JSODIMM2.85 (VSS), JSODIMM2.86 (VSS), JSODIMM2.89 (VSS), JSODIMM2.9 (VSS), JSODIMM2.90 (VSS), JSODIMM2.93 (VSS), JSODIMM2.94 (VSS), JSODIMM2.98 (VSS), JSODIMM2.99 (VSS), JSODIMM2.MP1, JSODIMM2.MP2

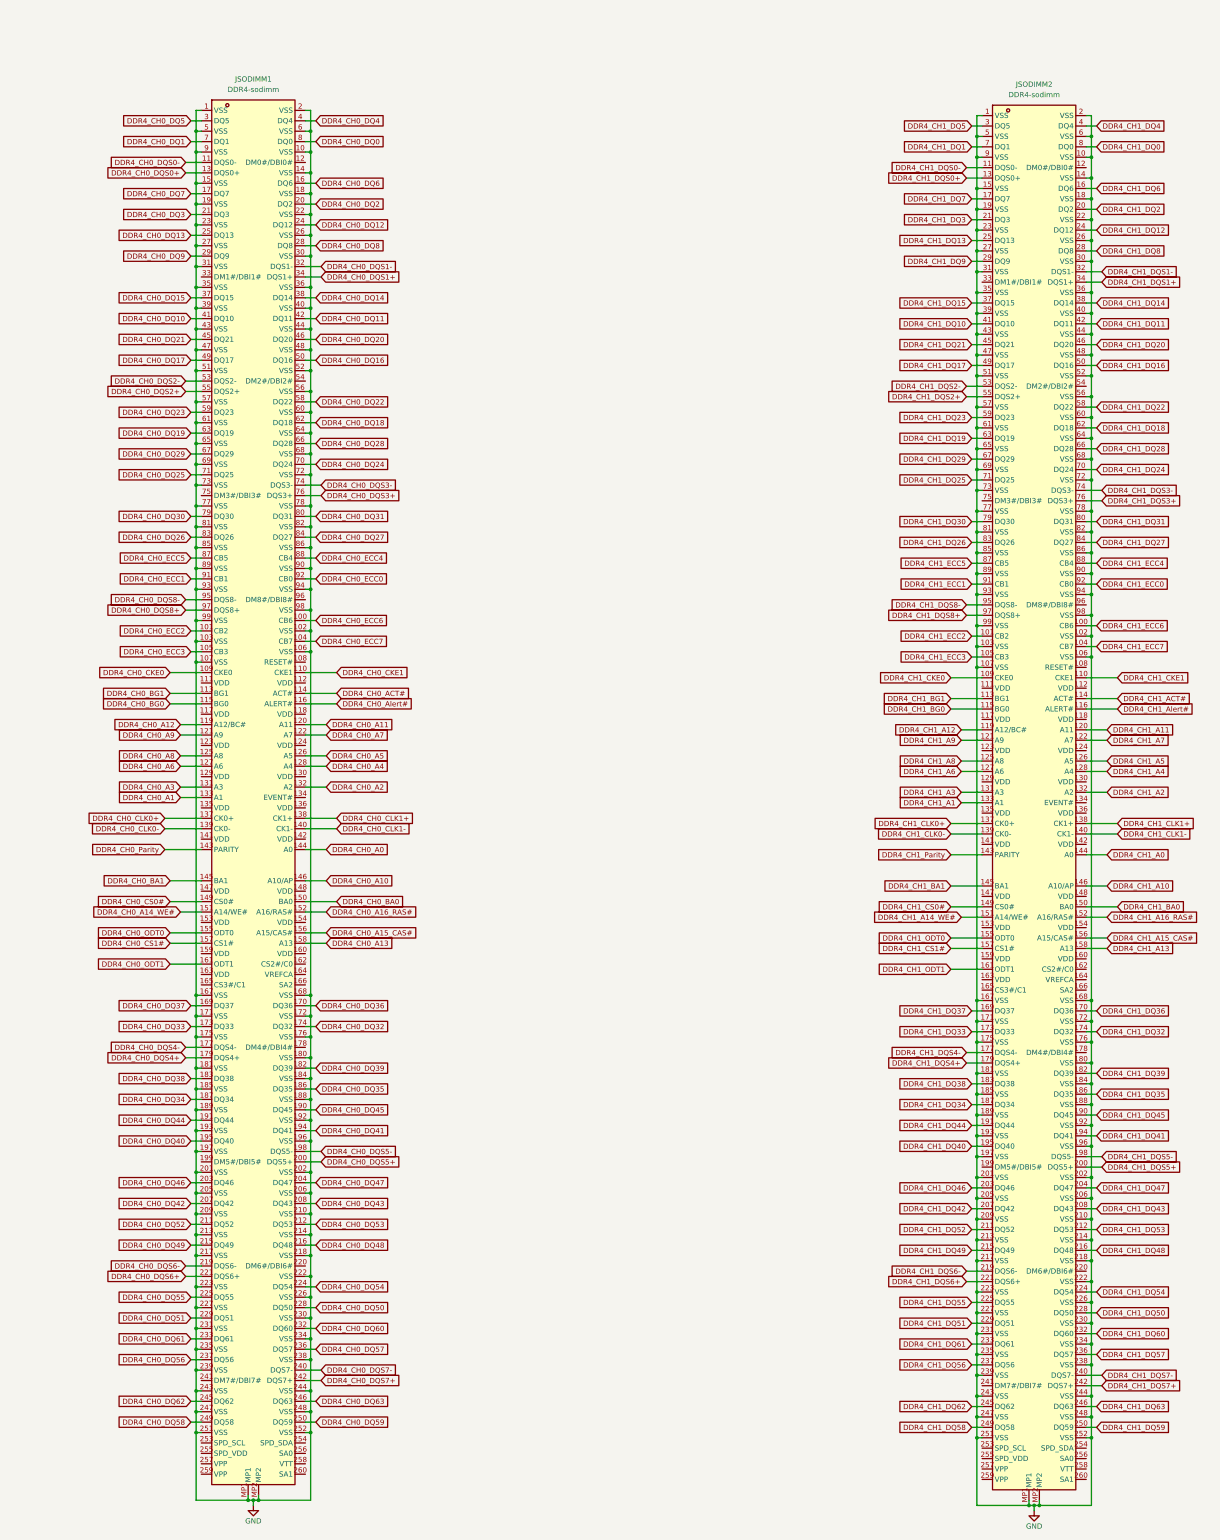
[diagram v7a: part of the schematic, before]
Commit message: Added DP_A DP++ HDMI dongle detection circuit
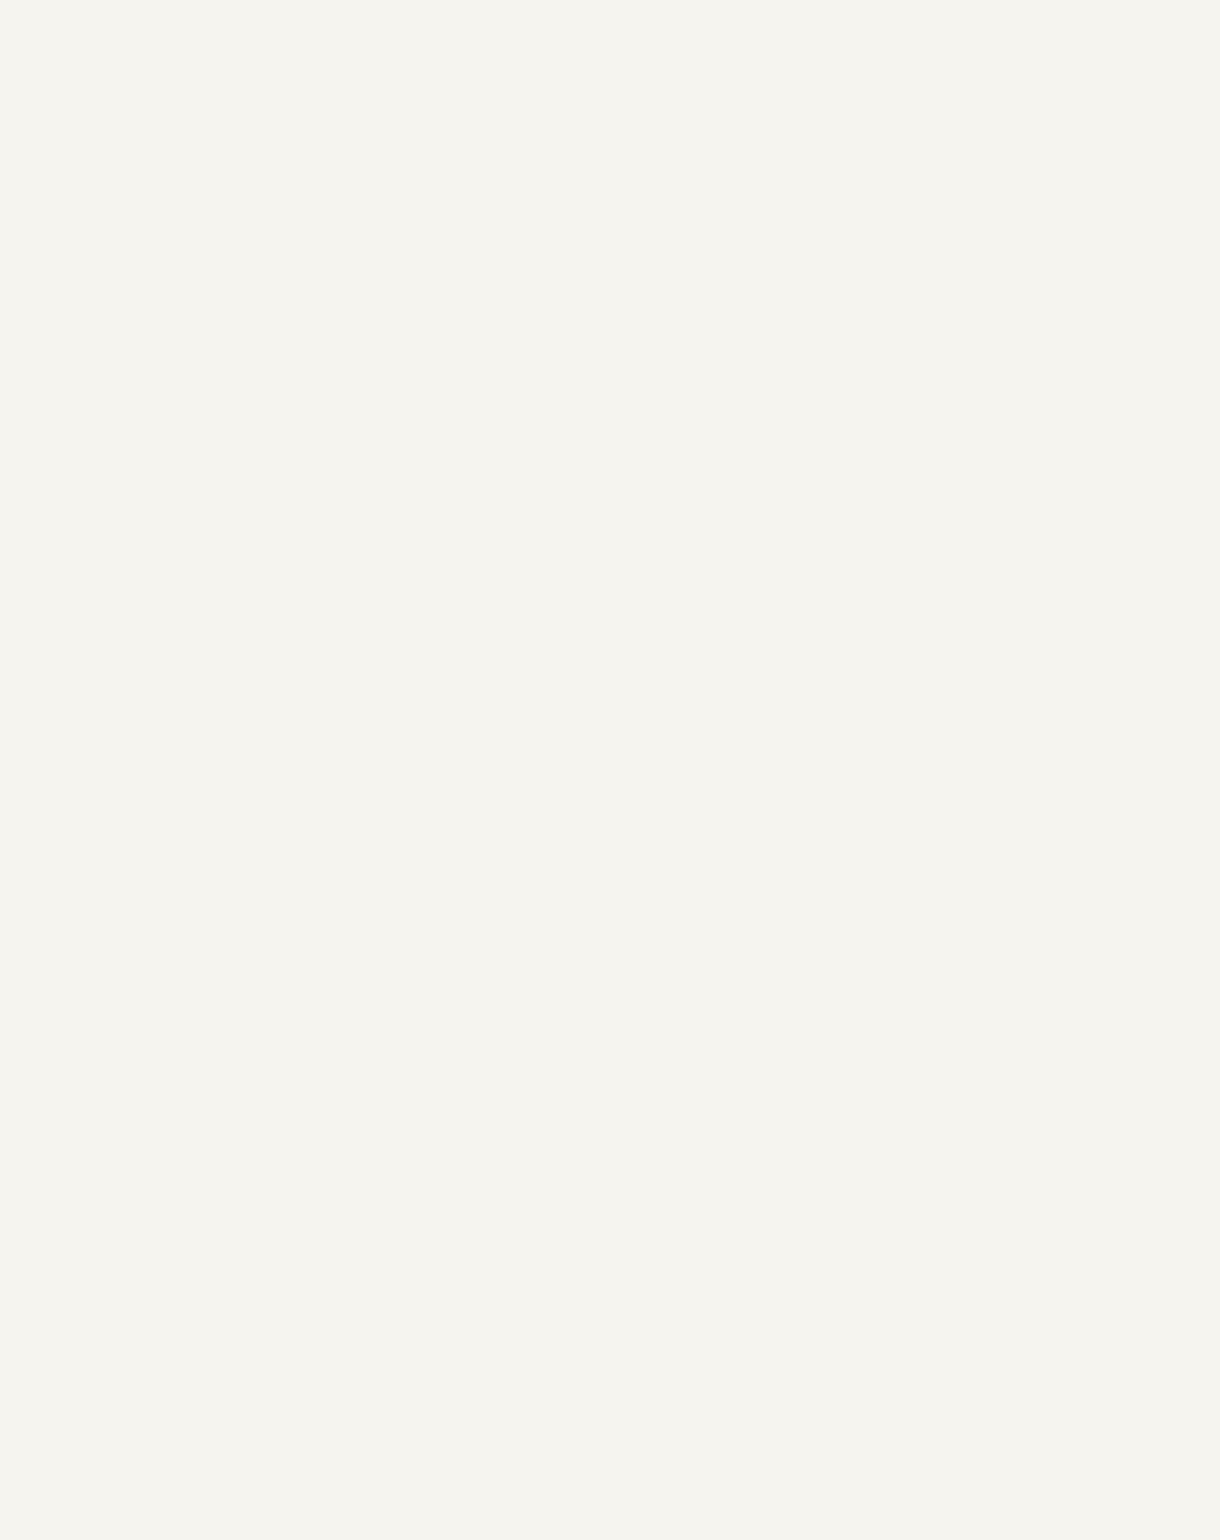
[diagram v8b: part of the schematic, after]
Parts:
- removed JSODIMM1, JSODIMM2: DDR4-sodimm, A-my-stuff:DDR4-sodimm-std, symbol A-my-stuff:DDR4-sodimm
